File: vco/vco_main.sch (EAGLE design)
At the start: 101 parts, among them IC1 OPA4130U, IC2 LM13700M, IC3 OPA4130U, IC4 OPA4130U, Q1 MMBFJ3

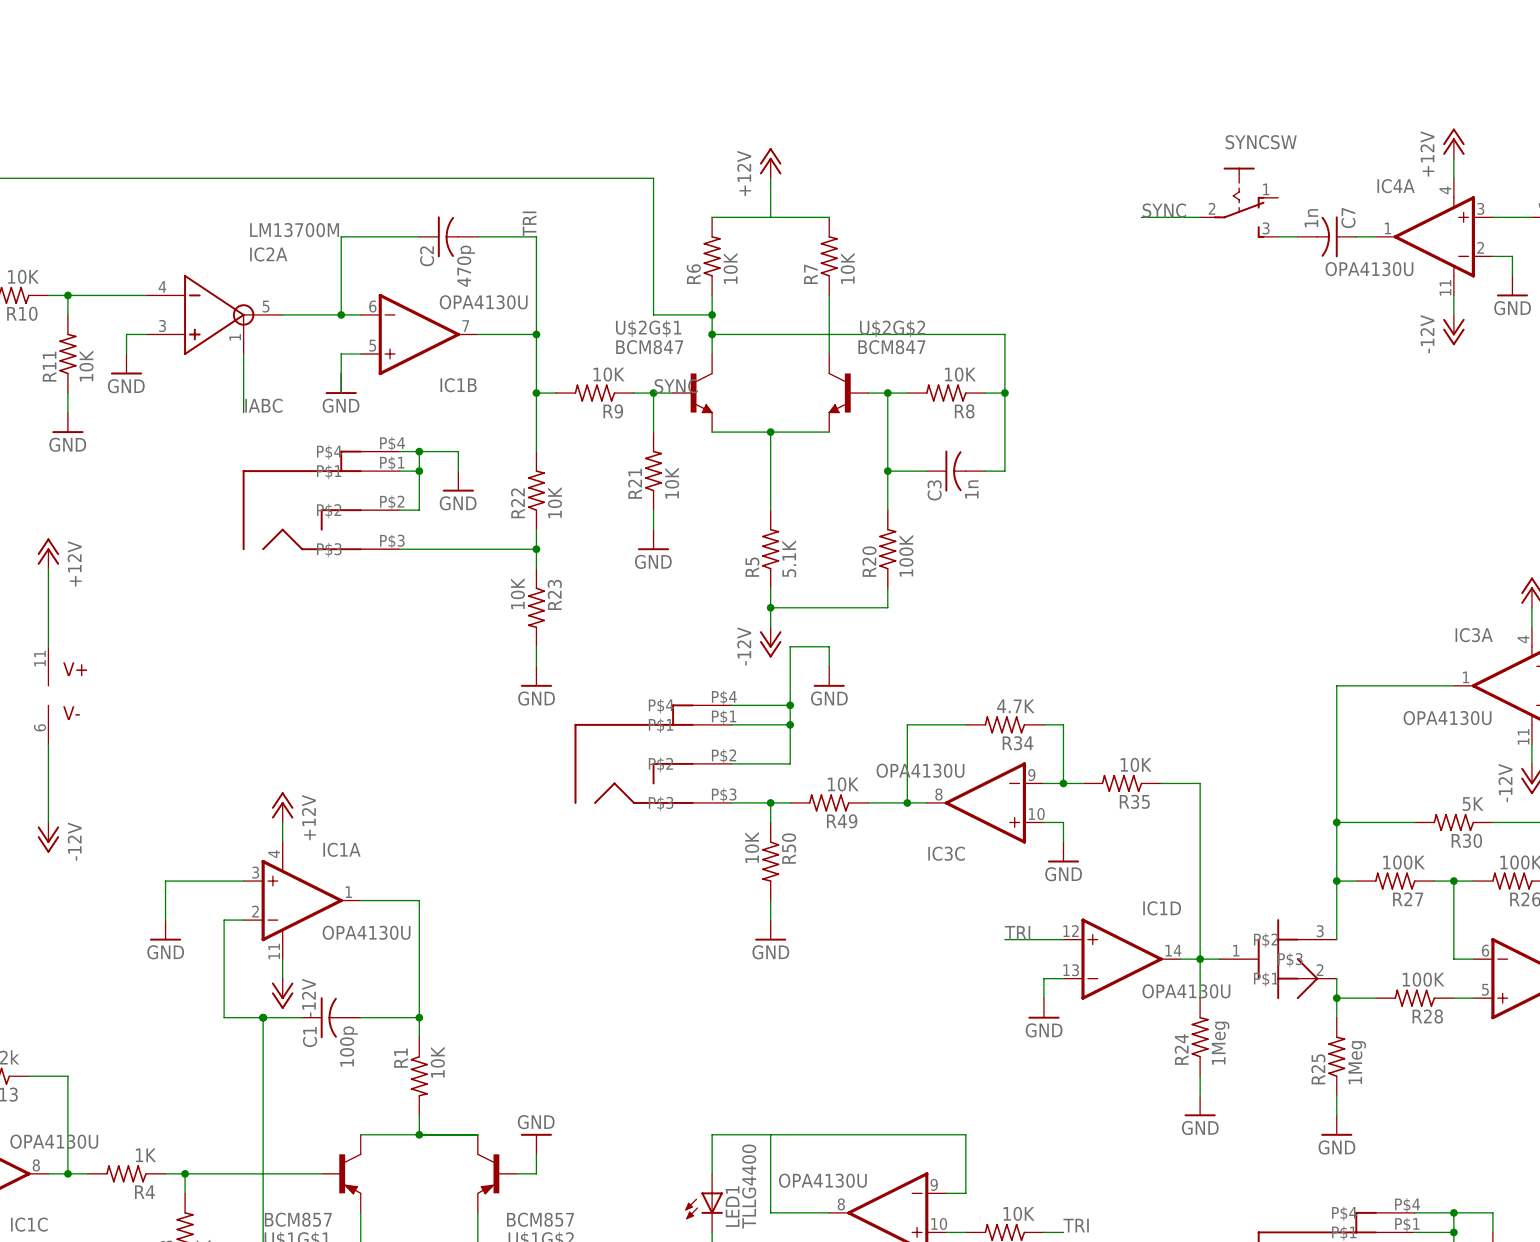
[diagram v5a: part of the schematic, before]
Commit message: added some to do notes to the schematic for final checking.
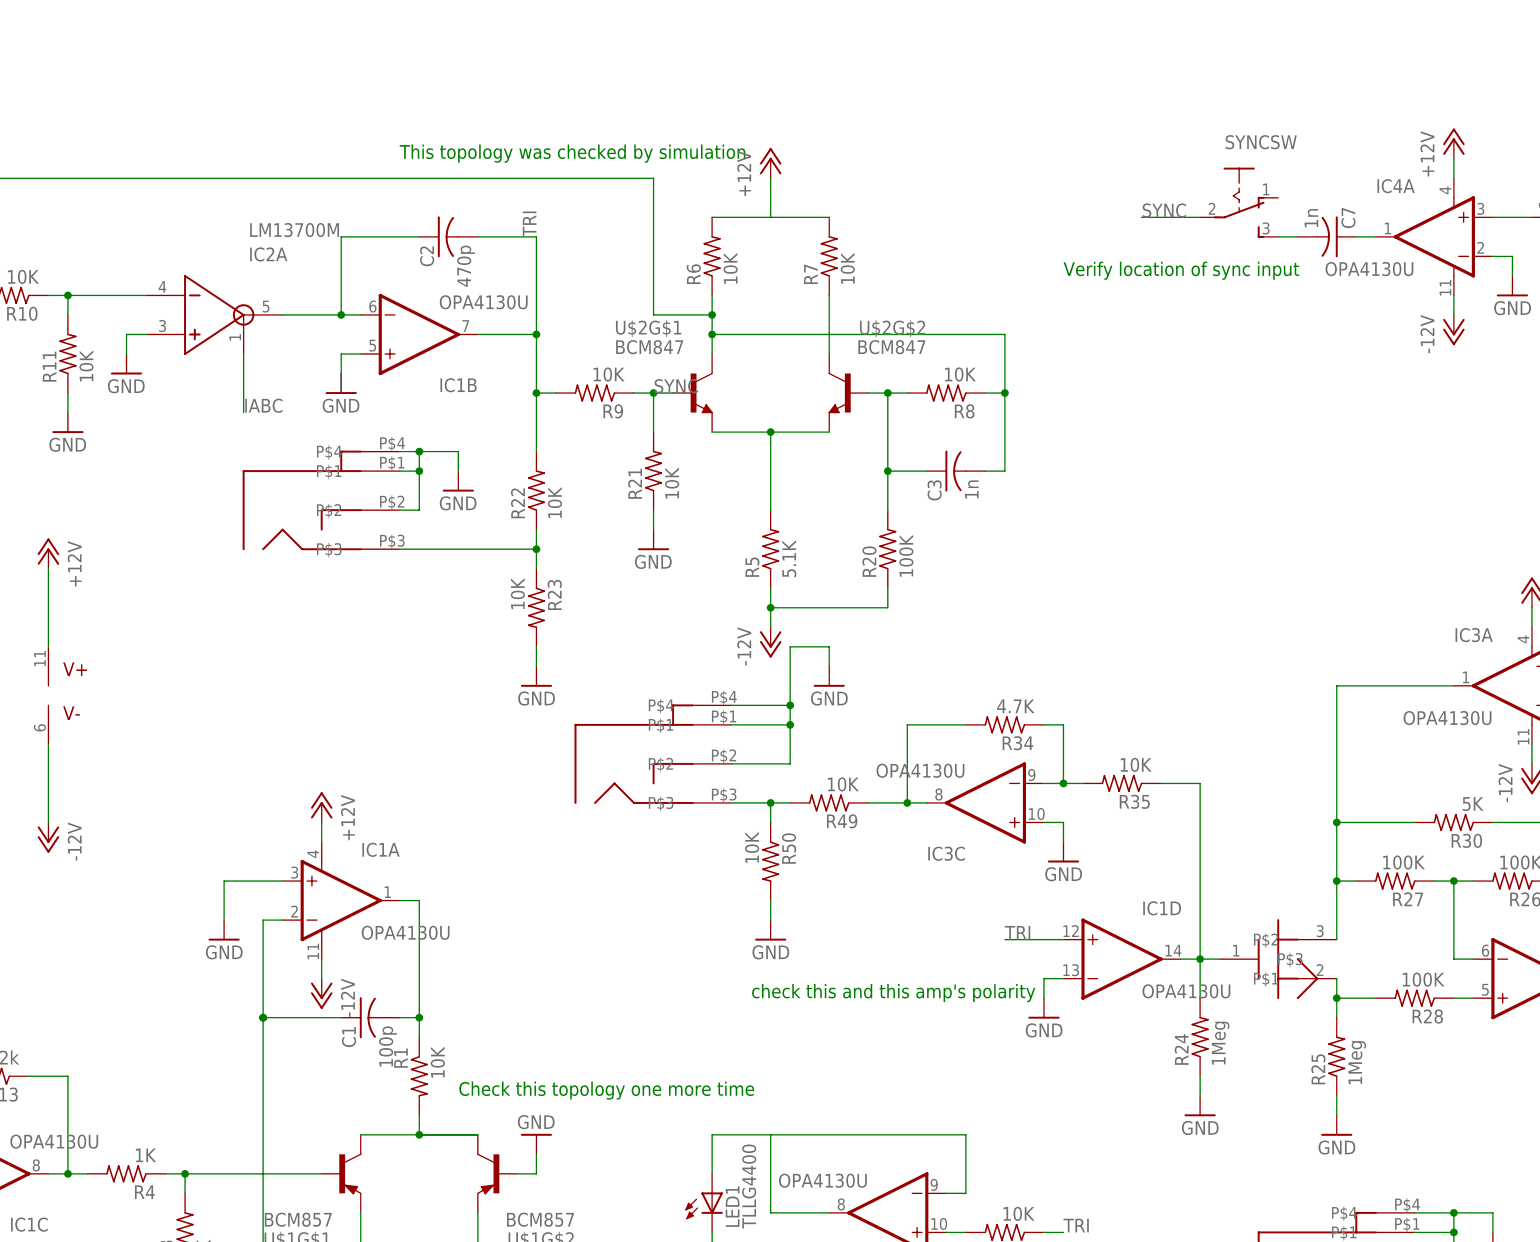
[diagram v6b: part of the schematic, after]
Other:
- note added: "Check this topology one more time"
- note added: "This topology was checked by simulation"
- note added: "Verify location of sync input"
- note added: "check this and this amp's polarity"
- moved on the sheet: C1, IC1A
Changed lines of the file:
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@@
 <sheet>
 <plain>
+<text x="124.46" y="38.1" size="1.778" layer="91">check this and this amp's polarity</text>
+<text x="78.74" y="147.32" size="1.778" layer="91">This topology was checked by simulation</text>
+<text x="86.36" y="25.4" size="1.778" layer="91">Check this topology one more time</text>
+<text x="165.1" y="132.08" size="1.778" layer="91">Verify location of sync input</text>
 </plain>
 <instances>
 <instance part="U$1" gate="G$1" x="71.12" y="15.24" rot="MR180"/>
 <instance part="U$1" gate="G$2" x="91.44" y="15.24" rot="R180"/>
-<instance part="IC1" gate="A" x="66.04" y="50.8"/>
+<instance part="IC1" gate="A" x="71.12" y="50.8"/>
 <instance part="IC1" gate="B" x="81.28" y="124.46" rot="MR180"/>
 <instance part="IC1" gate="C" x="25.4" y="15.24" rot="MR180"/>
@@
 <instance part="R1" gate="G$1" x="81.28" y="27.94" rot="MR270"/>
 <instance part="R2" gate="G$1" x="88.9" y="-15.24" rot="MR90"/>
-<instance part="GND1" gate="1" x="48.26" y="45.72" rot="MR0"/>
-<instance part="P+1" gate="1" x="63.5" y="63.5" rot="MR0"/>
-<instance part="P-1" gate="1" x="63.5" y="38.1" rot="MR0"/>
+<instance part="GND1" gate="1" x="55.88" y="45.72" rot="MR0"/>
+<instance part="P+1" gate="1" x="68.58" y="63.5" rot="MR0"/>
+<instance part="P-1" gate="1" x="68.58" y="38.1" rot="MR0"/>
 <instance part="GND2" gate="1" x="96.52" y="20.32" rot="MR180"/>
 <instance part="R3" gate="G$1" x="50.8" y="7.62" rot="R90"/>
@@
 <instance part="IC2" gate="G$3" x="-91.44" y="71.12"/>
 <instance part="IC2" gate="G$4" x="-91.44" y="63.5"/>
-<instance part="C1" gate="G$1" x="68.58" y="35.56" rot="MR270"/>
+<instance part="C1" gate="G$1" x="73.66" y="35.56" rot="MR270"/>
 <instance part="FINE" gate="G$1" x="-48.26" y="27.94"/>
 <instance part="R14" gate="G$1" x="-48.26" y="43.18" rot="R90"/>
@@
 <pinref part="IC1" gate="A" pin="OUT"/>
 <pinref part="R1" gate="G$1" pin="1"/>
-<wire x1="73.66" y1="50.8" x2="81.28" y2="50.8" width="0.1524" layer="91"/>
+<wire x1="78.74" y1="50.8" x2="81.28" y2="50.8" width="0.1524" layer="91"/>
 <wire x1="81.28" y1="50.8" x2="81.28" y2="35.56" width="0.1524" layer="91"/>
 <pinref part="C1" gate="G$1" pin="2"/>
 <wire x1="81.28" y1="35.56" x2="81.28" y2="33.02" width="0.1524" layer="91"/>
-<wire x1="73.66" y1="35.56" x2="81.28" y2="35.56" width="0.1524" layer="91"/>
+<wire x1="78.74" y1="35.56" x2="81.28" y2="35.56" width="0.1524" layer="91"/>
 <junction x="81.28" y="35.56"/>
 </segment>
@@
 <segment>
 <pinref part="IC1" gate="A" pin="-IN"/>
-<wire x1="58.42" y1="48.26" x2="55.88" y2="48.26" width="0.1524" layer="91"/>
-<wire x1="55.88" y1="48.26" x2="55.88" y2="35.56" width="0.1524" layer="91"/>
+<wire x1="63.5" y1="48.26" x2="60.96" y2="48.26" width="0.1524" layer="91"/>
+<wire x1="60.96" y1="48.26" x2="60.96" y2="35.56" width="0.1524" layer="91"/>
 <pinref part="C1" gate="G$1" pin="1"/>
-<wire x1="66.04" y1="35.56" x2="60.96" y2="35.56" width="0.1524" layer="91"/>
+<wire x1="71.12" y1="35.56" x2="60.96" y2="35.56" width="0.1524" layer="91"/>
 <pinref part="C5" gate="G$1" pin="1"/>
 <wire x1="60.96" y1="-7.62" x2="60.96" y2="-5.08" width="0.1524" layer="91"/>
@@
 <wire x1="88.9" y1="-5.08" x2="88.9" y2="-10.16" width="0.1524" layer="91"/>
 <junction x="88.9" y="-5.08"/>
-<wire x1="55.88" y1="35.56" x2="60.96" y2="35.56" width="0.1524" layer="91"/>
 <wire x1="60.96" y1="35.56" x2="60.96" y2="-5.08" width="0.1524" layer="91"/>
 <junction x="60.96" y="-5.08"/>
@@
 <segment>
 <pinref part="IC1" gate="A" pin="V-"/>
-<wire x1="63.5" y1="43.18" x2="63.5" y2="40.64" width="0.1524" layer="91"/>
+<wire x1="68.58" y1="43.18" x2="68.58" y2="40.64" width="0.1524" layer="91"/>
 <pinref part="P-1" gate="1" pin="-12V"/>
 </segment>
@@
 <segment>
 <pinref part="IC1" gate="A" pin="V+"/>
-<wire x1="63.5" y1="58.42" x2="63.5" y2="60.96" width="0.1524" layer="91"/>
+<wire x1="68.58" y1="58.42" x2="68.58" y2="60.96" width="0.1524" layer="91"/>
 <pinref part="P+1" gate="1" pin="+12V"/>
 </segment>
@@
 <segment>
 <pinref part="GND1" gate="1" pin="GND"/>
-<wire x1="48.26" y1="48.26" x2="48.26" y2="53.34" width="0.1524" layer="91"/>
+<wire x1="55.88" y1="48.26" x2="55.88" y2="53.34" width="0.1524" layer="91"/>
 <pinref part="IC1" gate="A" pin="+IN"/>
-<wire x1="48.26" y1="53.34" x2="58.42" y2="53.34" width="0.1524" layer="91"/>
-</segment>
-<segment>
+<wire x1="55.88" y1="53.34" x2="63.5" y2="53.34" width="0.1524" layer="91"/>
+</segment>
+<segment>

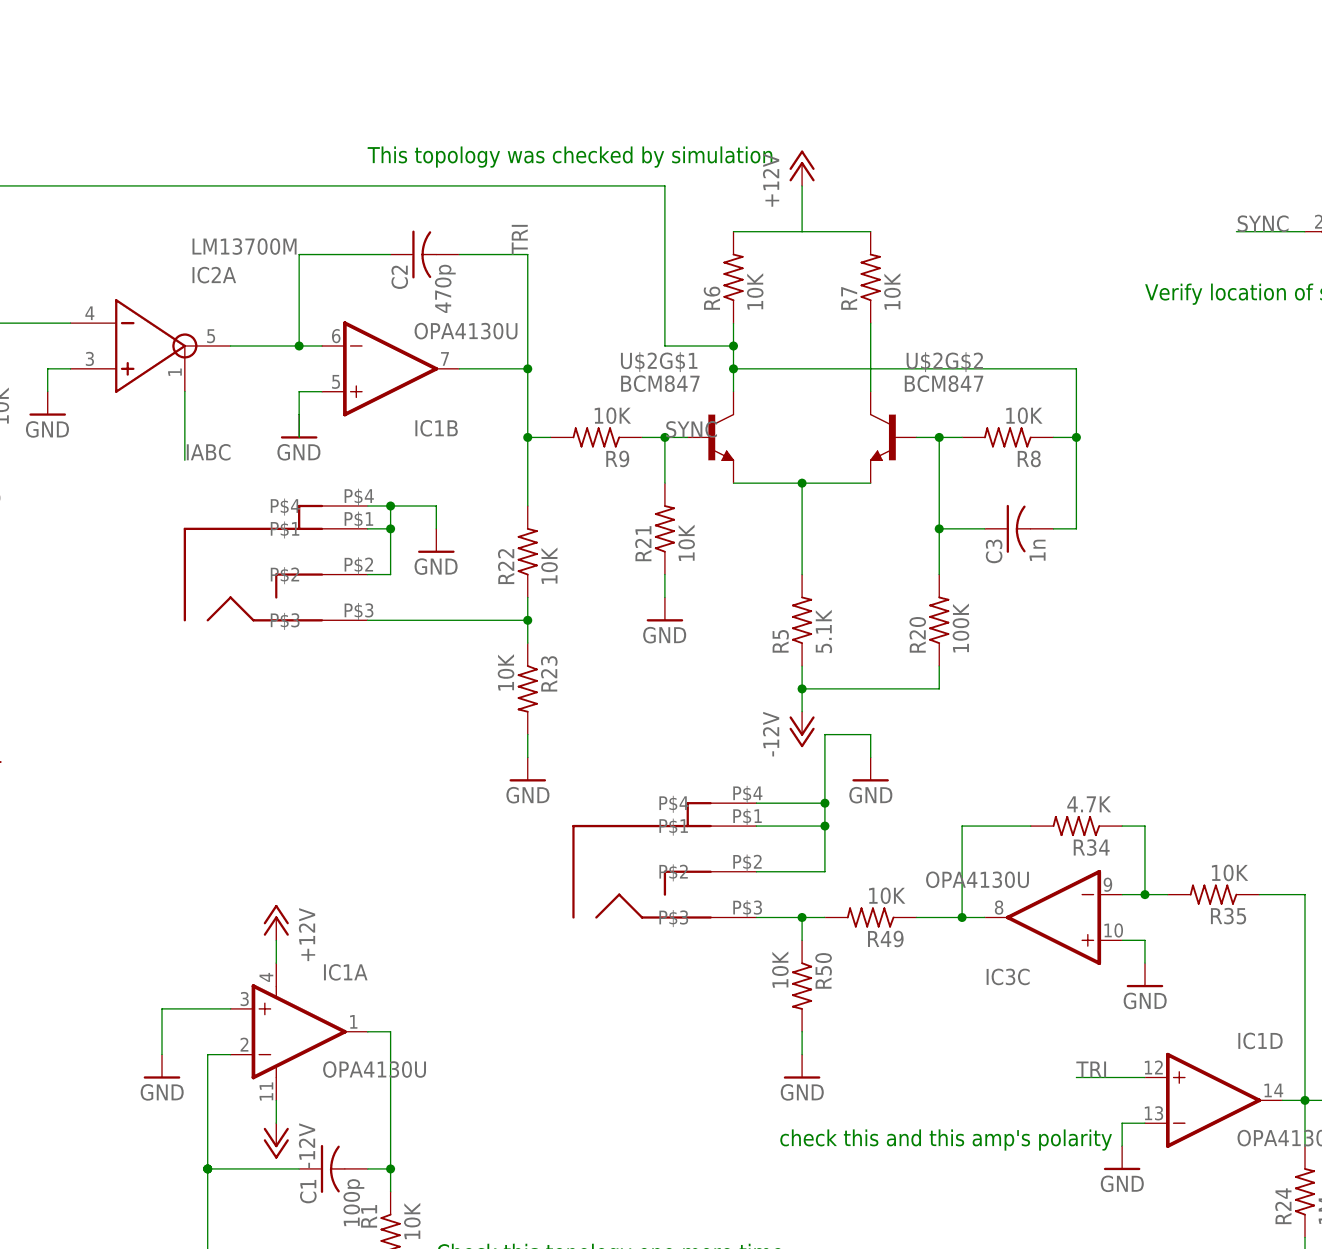
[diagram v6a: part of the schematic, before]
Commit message: fixed a serious problem with the saw.  cleaned some nets up.
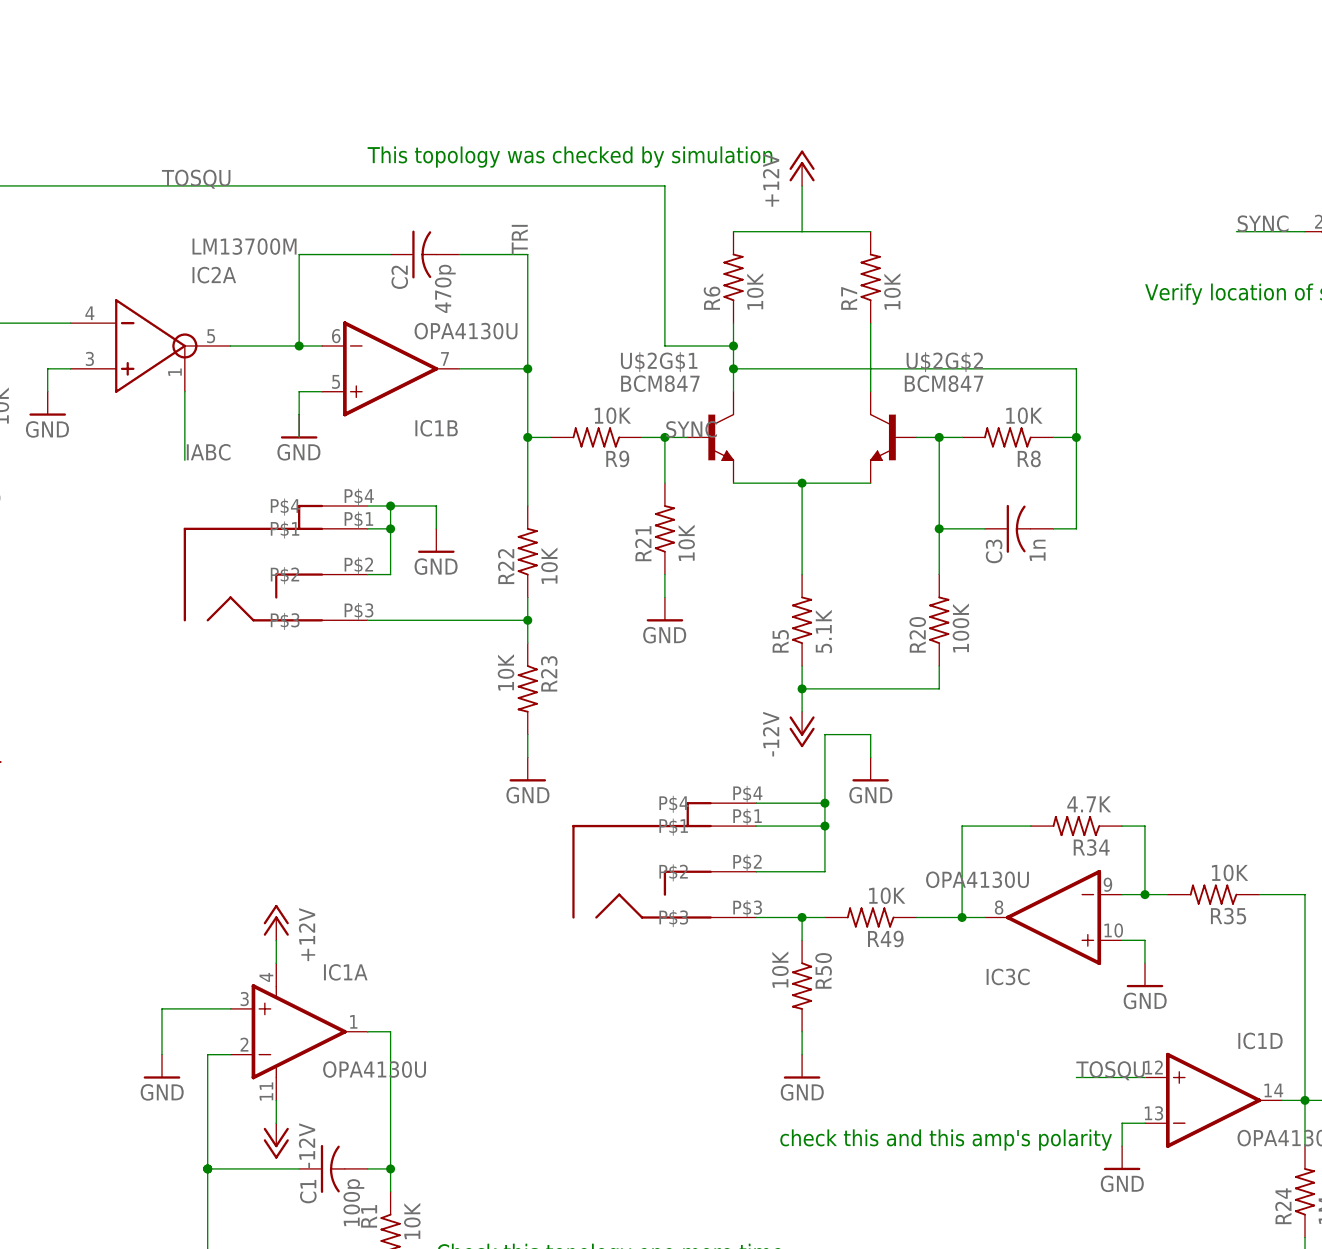
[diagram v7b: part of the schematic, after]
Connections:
- removed net N$12: C3.2, R10.2, R6.1, R8.1, U$2G$1.C
- new net TOSQU: C3.2, IC1D.+IN, R10.2, R6.1, R8.1, U$2G$1.C
- net TRI: no longer IC1D.+IN
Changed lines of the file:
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@@
-</segment>
-<segment>
-<pinref part="IC1" gate="D" pin="+IN"/>
-<wire x1="165.1" y1="45.72" x2="157.48" y2="45.72" width="0.1524" layer="91"/>
-<label x="157.48" y="45.72" size="1.778" layer="95"/>
 </segment>
 <segment>
@@
 </segment>
 </net>
-<net name="N$12" class="0">
+<net name="TOSQU" class="0">
 <segment>
 <pinref part="R6" gate="G$1" pin="1"/>
@@
 <wire x1="111.76" y1="144.78" x2="20.32" y2="144.78" width="0.1524" layer="91"/>
 <junction x="119.38" y="127"/>
+<label x="55.88" y="144.78" size="1.778" layer="95"/>
+</segment>
+<segment>
+<pinref part="IC1" gate="D" pin="+IN"/>
+<wire x1="165.1" y1="45.72" x2="157.48" y2="45.72" width="0.1524" layer="91"/>
+<label x="157.48" y="45.72" size="1.778" layer="95"/>
 </segment>
 </net>
